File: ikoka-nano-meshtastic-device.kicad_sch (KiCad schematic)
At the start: 21 parts, among them J1 Qwiic_RA, J2 Solar, J3 Battery, J4 Battery, Q1 Q_PMOS_GSD, U1 Seeed Studio XIAO nRF52840, U2 E22-900M30S, U3 MT3608

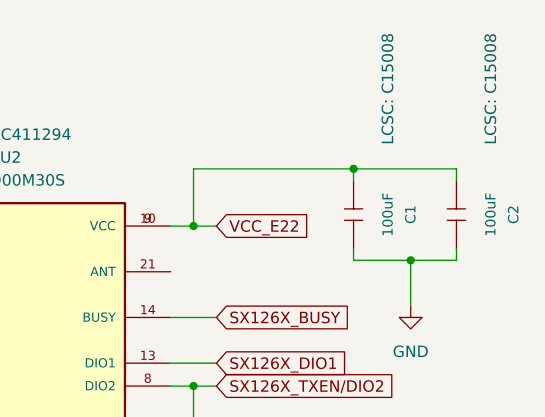
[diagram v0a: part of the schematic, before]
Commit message: Sync symbol libraries
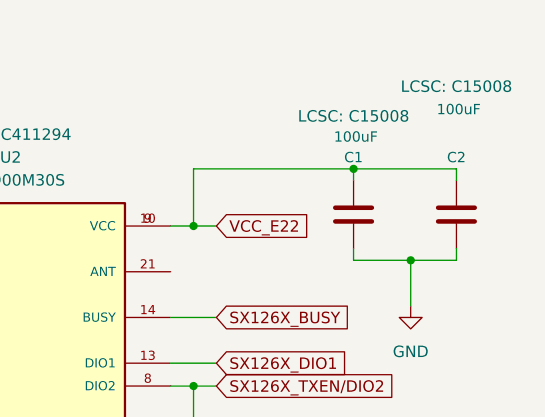
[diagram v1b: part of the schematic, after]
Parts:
- C1, C2: symbol OPL_Capacitor:CERAMIC-100UF-6.3V-20%-X5R_1206_ -> Device:C
- J1: footprint SparkFun-Connector:JST_SMD_1.0mm-4_RA -> SparkFun-Connector:JST_SMD_1.0mm-4_Black
- U2: Description_1 (none) -> SX1262 868/915 MHz 1w SPI LoRa Module
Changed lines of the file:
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@@
 	)
 	(symbol
-		(lib_name "GND_2")
 		(lib_id "power:GND")
 		(at 147.32 181.61 0)
@@
 			)
 		)
-		(property "Description" ""
+		(property "Description" "Power symbol creates a global label with name \"GND\" , ground"
 			(at 250.19 59.69 0)
 			(effects
@@
 			)
 		)
-		(property "Description" ""
+		(property "Description" "Power symbol creates a global label with name \"GND\" , ground"
 			(at 123.19 83.82 0)
 			(effects
@@
 			)
 		)
-		(property "Footprint" "SparkFun-Connector:JST_SMD_1.0mm-4_RA"
+		(property "Footprint" "SparkFun-Connector:JST_SMD_1.0mm-4_Black"
 			(at 53.34 180.34 0)
 			(effects
@@
 	)
 	(symbol
-		(lib_id "OPL_Capacitor:CERAMIC-100UF-6.3V-20%-X5R_1206_")
-		(at 255.27 49.53 90)
+		(lib_id "Device:C")
+		(at 255.27 49.53 180)
 		(unit 1)
 		(exclude_from_sim no)
@@
 		(dnp no)
 		(property "Reference" "C2"
-			(at 261.62 49.53 0)
+			(at 255.27 43.18 0)
 			(effects
 				(font
@@
 		)
 		(property "Value" "100uF"
-			(at 259.08 49.53 0)
+			(at 255.524 37.846 0)
 			(effects
 				(font
@@
 		)
 		(property "Footprint" "Capacitor_SMD:C_1206_3216Metric_Pad1.33x1.80mm_HandSolder"
+			(at 254.3048 45.72 0)
+			(effects
+				(font
+					(size 1.27 1.27)
+				)
+				(hide yes)
+			)
+		)
+		(property "Datasheet" "~"
 			(at 255.27 49.53 0)
 			(effects
@@
 			)
 		)
-		(property "Datasheet" ""
+		(property "Description" "Unpolarized capacitor"
 			(at 255.27 49.53 0)
 			(effects
@@
 			)
 		)
-		(property "Description" ""
-			(at 255.27 49.53 0)
-			(effects
-				(font
-					(size 1.27 1.27)
-				)
-				(hide yes)
-			)
-		)
 		(property "MPN" "CL31A107MQHNNNE"
-			(at 251.46 48.768 0)
+			(at 254.508 53.34 0)
 			(effects
 				(font
@@
 		)
 		(property "LCSC" "C15008"
-			(at 259.08 35.56 0)
+			(at 255.27 35.306 0)
 			(show_name yes)
 			(effects
@@
 	)
 	(symbol
-		(lib_name "GND_3")
 		(lib_id "power:GND")
 		(at 194.31 135.89 0)
@@
 			)
 		)
-		(property "Description" ""
+		(property "Description" "Power symbol creates a global label with name \"GND\" , ground"
 			(at 228.6 83.82 0)
 			(effects
@@
 			)
 		)
+		(property "Description_1" "\nSX1262 868/915 MHz 1w SPI LoRa Module\n"
+			(at 205.74 63.5 0)
+			(effects
+				(font
+					(size 1.27 1.27)
+				)
+				(justify bottom)
+				(hide yes)
+			)
+		)
 		(pin "8"
 		)
@@
 	)
 	(symbol
-		(lib_name "GND_1")
 		(lib_id "power:GND")
 		(at 90.17 184.15 0)
@@
 	)
 	(symbol
-		(lib_id "OPL_Capacitor:CERAMIC-100UF-6.3V-20%-X5R_1206_")
-		(at 243.84 49.53 90)
+		(lib_id "Device:C")
+		(at 243.84 49.53 180)
 		(unit 1)
 		(exclude_from_sim no)
@@
 		(dnp no)
 		(property "Reference" "C1"
-			(at 250.19 49.53 0)
+			(at 243.84 43.18 0)
 			(effects
 				(font
@@
 		)
 		(property "Value" "100uF"
-			(at 247.65 49.53 0)
+			(at 244.094 40.894 0)
 			(effects
 				(font
@@
 		)
 		(property "Footprint" "Capacitor_SMD:C_1206_3216Metric_Pad1.33x1.80mm_HandSolder"
+			(at 242.8748 45.72 0)
+			(effects
+				(font
+					(size 1.27 1.27)
+				)
+				(hide yes)
+			)
+		)
+		(property "Datasheet" "~"
 			(at 243.84 49.53 0)
 			(effects
@@
 			)
 		)
-		(property "Datasheet" ""
+		(property "Description" "Unpolarized capacitor"
 			(at 243.84 49.53 0)
 			(effects
@@
 			)
 		)
-		(property "Description" ""
-			(at 243.84 49.53 0)
-			(effects
-				(font
-					(size 1.27 1.27)
-				)
-				(hide yes)
-			)
-		)
 		(property "MPN" "CL31A107MQHNNNE"
-			(at 240.03 48.768 0)
+			(at 243.078 53.34 0)
 			(effects
 				(font
@@
 		)
 		(property "LCSC" "C15008"
-			(at 247.65 35.56 0)
+			(at 243.84 38.608 0)
 			(show_name yes)
 			(effects

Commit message: chore: Sync footprint libraries
Signed-off-by: Andrew Yong <me@ndoo.sg>
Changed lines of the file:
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@@
 (kicad_sch
-	(version 20231120)
+	(version 20250114)
 	(generator "eeschema")
-	(generator_version "8.0")
+	(generator_version "9.0")
 	(paper "A4")
 	(title_block
@@
 		(company "ndoo.sg")
 	)
+	(text "Nominal Vout: 5.4V"
+		(exclude_from_sim no)
+		(at 229.108 122.174 0)
+		(effects
+			(font
+				(size 1.27 1.27)
+			)
+		)
+	)
+	(text "Normally, gate would be pulled to ground to prevent floating.\nIn this case, VBUS is not pulled to ground because there is internal 100k pulldown on XIAO BLE.\nhttps://files.seeedstudio.com/wiki/XIAO-BLE/Seeed-Studio-XIAO-nRF52840-Sense-v1.1.pdf"
+		(exclude_from_sim no)
+		(at 109.22 133.35 0)
+		(effects
+			(font
+				(size 1.27 1.27)
+			)
+		)
+	)
 	(junction
 		(at 217.17 134.62)
@@
 		)
 	)
-	(text "Nominal Vout: 5.4V"
-		(exclude_from_sim no)
-		(at 229.108 122.174 0)
-		(effects
-			(font
-				(size 1.27 1.27)
-			)
-		)
-	)
-	(text "Normally, gate would be pulled to ground to prevent floating.\nIn this case, VBUS is not pulled to ground because there is internal 100k pulldown on XIAO BLE.\nhttps://files.seeedstudio.com/wiki/XIAO-BLE/Seeed-Studio-XIAO-nRF52840-Sense-v1.1.pdf"
-		(exclude_from_sim no)
-		(at 109.22 133.35 0)
-		(effects
-			(font
-				(size 1.27 1.27)
-			)
-		)
-	)
 	(global_label "VBAT"
 		(shape input)
@@
 		)
 	)
+	(embedded_fonts no)
 )

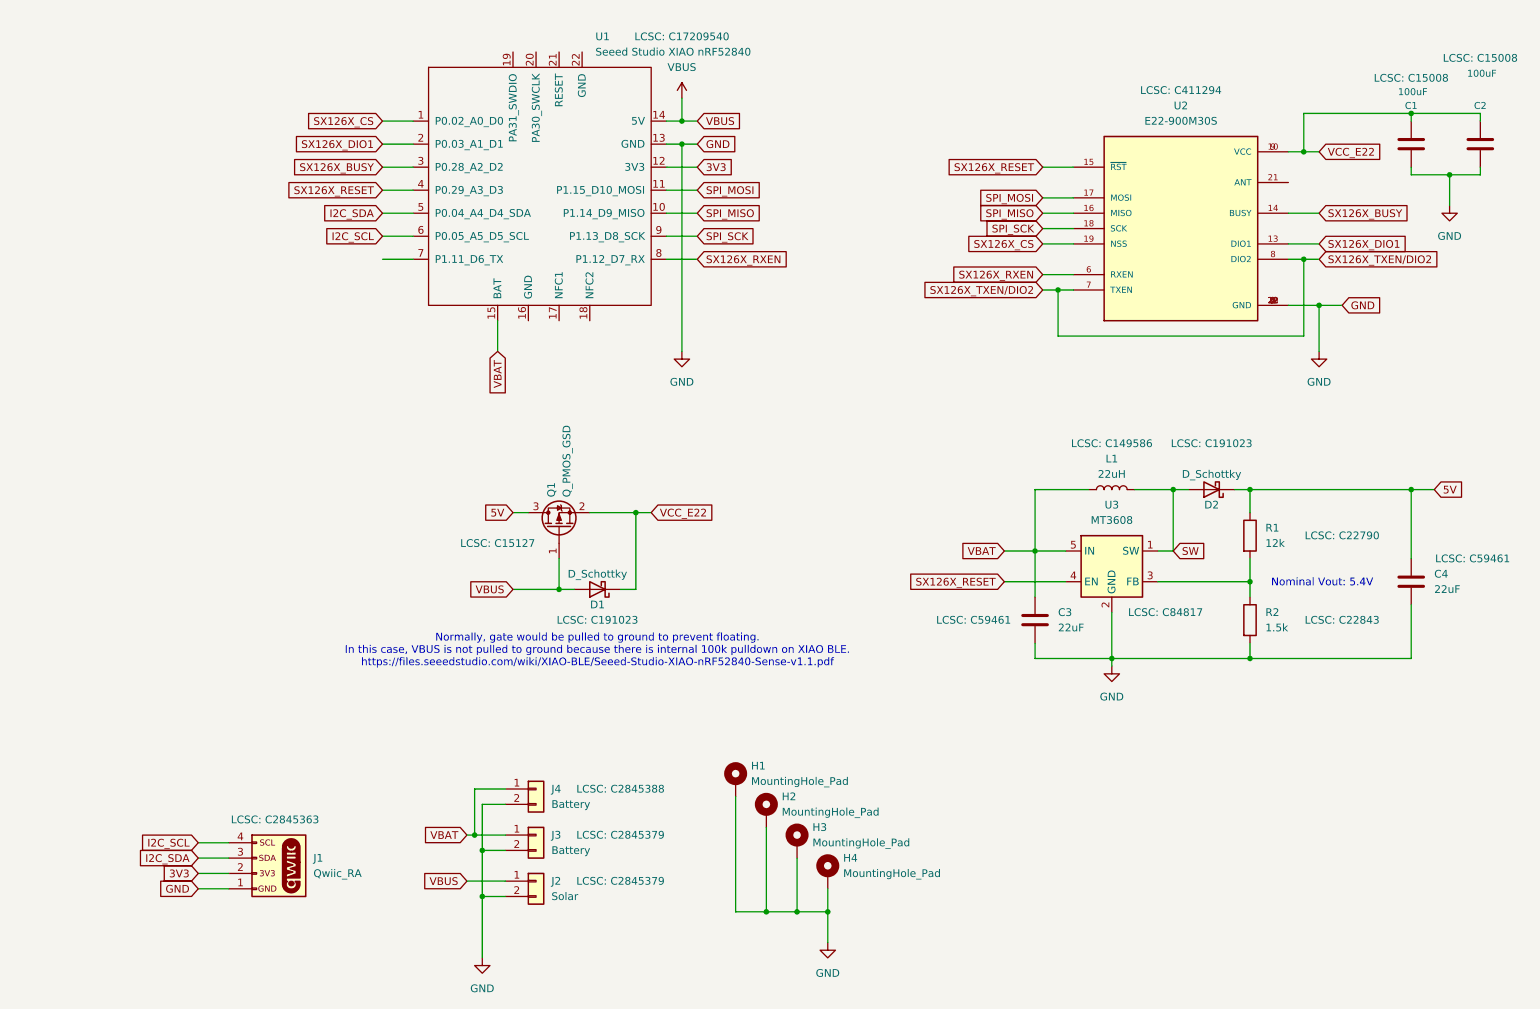
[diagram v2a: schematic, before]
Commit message: feat: Improve DC-DC converter and power path
- Update R1 and R2 resistors to match Ikoka Handheld values (300kΩ, 39kΩ respectively)
- Change E22 capacitors to 2x 47µF instead of 2x 100µF
- Change P-MOSFET load switch to switch input to DC-DC boost so that E22 supply is constant even when switching to USB power
- Add 300k pulldown on MT3608L enable pin to prevent it floating when Meshtastic firmware is not running
- Layout for above changes
- Move connectors flush with PCB edge

Fixes #11

Signed-off-by: Andrew Yong <me@ndoo.sg>
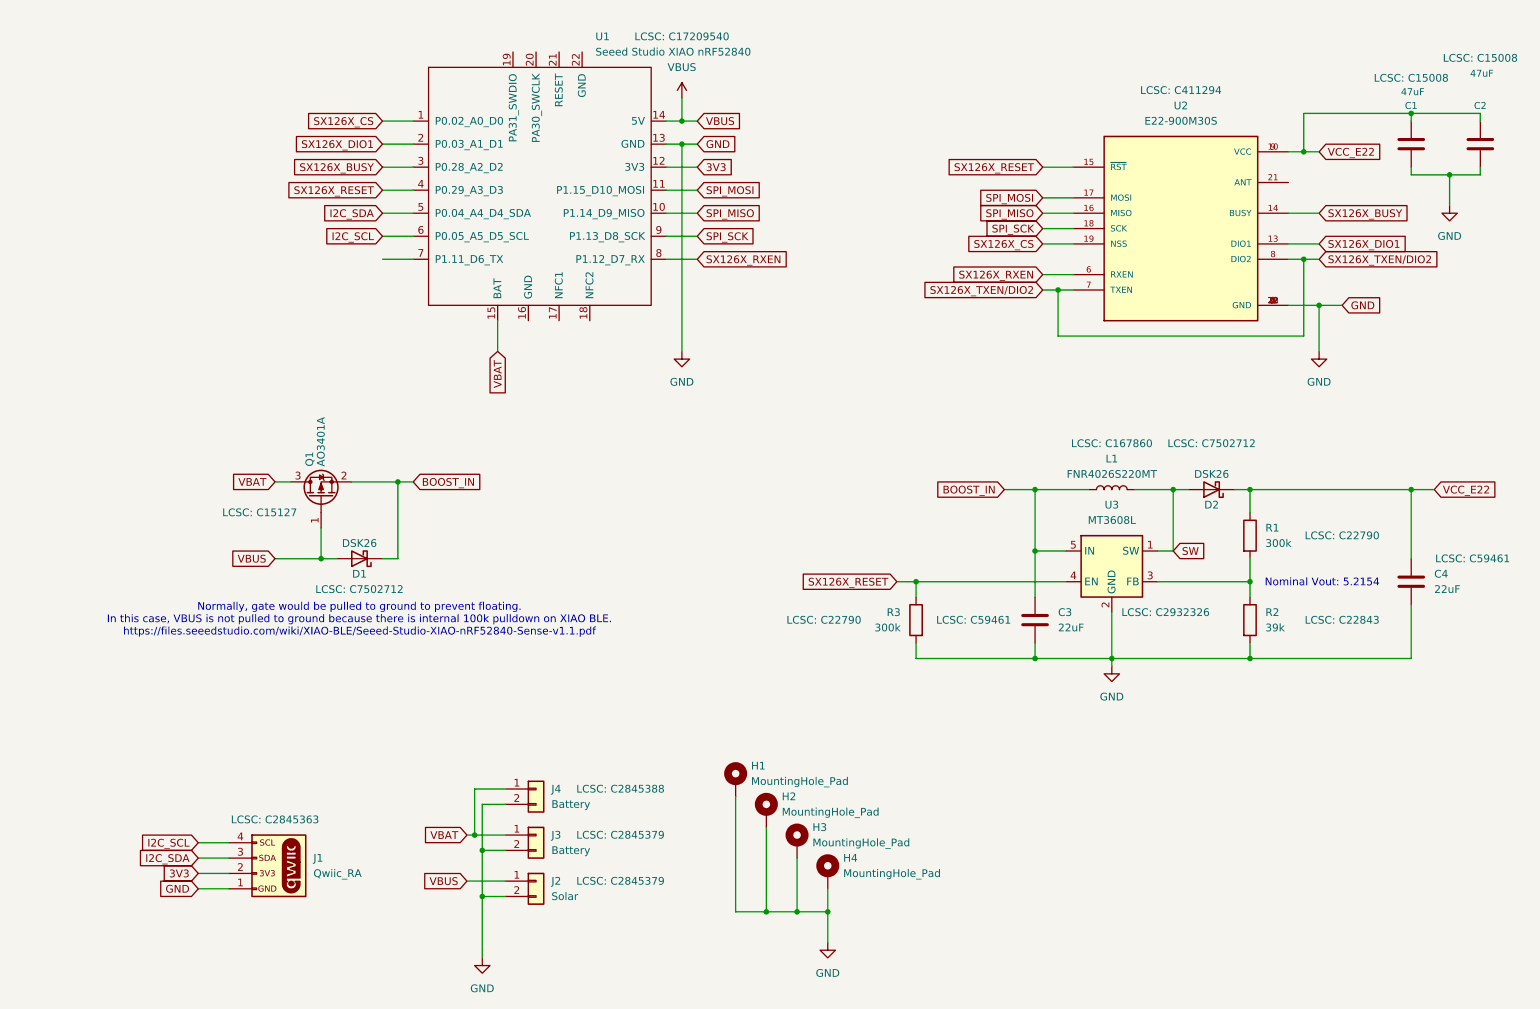
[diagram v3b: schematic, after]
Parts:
- added R3: 300k, Resistor_SMD:R_0603_1608Metric_Pad0.98x0.95mm_HandSolder, symbol Device:R
- C1, C2: value 100uF -> 47uF; footprint Capacitor_SMD:C_1206_3216Metric_Pad1.33x1.80mm_HandSolder -> Capacitor_SMD:C_0805_2012Metric_Pad1.18x1.45mm_HandSolder
- D1, D2: value D_Schottky -> DSK26; footprint Diode_SMD:D_SOD-323_HandSoldering -> Diode_SMD:D_SOD-123F; LCSC C191023 -> C7502712
- L1: value 22uH -> FNR4026S220MT; footprint Inductor_SMD:L_SXN_SMDRI64 -> Inductor_SMD:L_Changjiang_FNR4026S; LCSC C149586 -> C167860
- Q1: value Q_PMOS_GSD -> AO3401A; footprint Package_TO_SOT_SMD:SOT-23_Handsoldering -> Package_TO_SOT_SMD:SOT-23; symbol Device:Q_PMOS_GSD -> Transistor_FET:AO3401A
- R1: value 12k -> 300k
- R2: value 1.5k -> 39k
- U3: value MT3608 -> MT3608L; LCSC C84817 -> C2932326
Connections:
- net GND: now also R3.2
- net SX126X_RESET: now also R3.1
- net VBAT: now also Q1.3 (D); no longer C3.1, L1.1, U3.5 (IN)
- net VCC_E22: now also C4.1, D2.1 (K), R1.1; no longer D1.1 (K), Q1.2 (S)
- removed net 5V: C4.1, D2.1 (K), Q1.3 (D), R1.1
- new net BOOST_IN: C3.1, D1.1 (K), L1.1, Q1.2 (S), U3.5 (IN)
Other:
- note added: "Nominal Vout: 5.2154"
- note removed: "Nominal Vout: 5.4V"
- moved on the sheet: D1, Q1

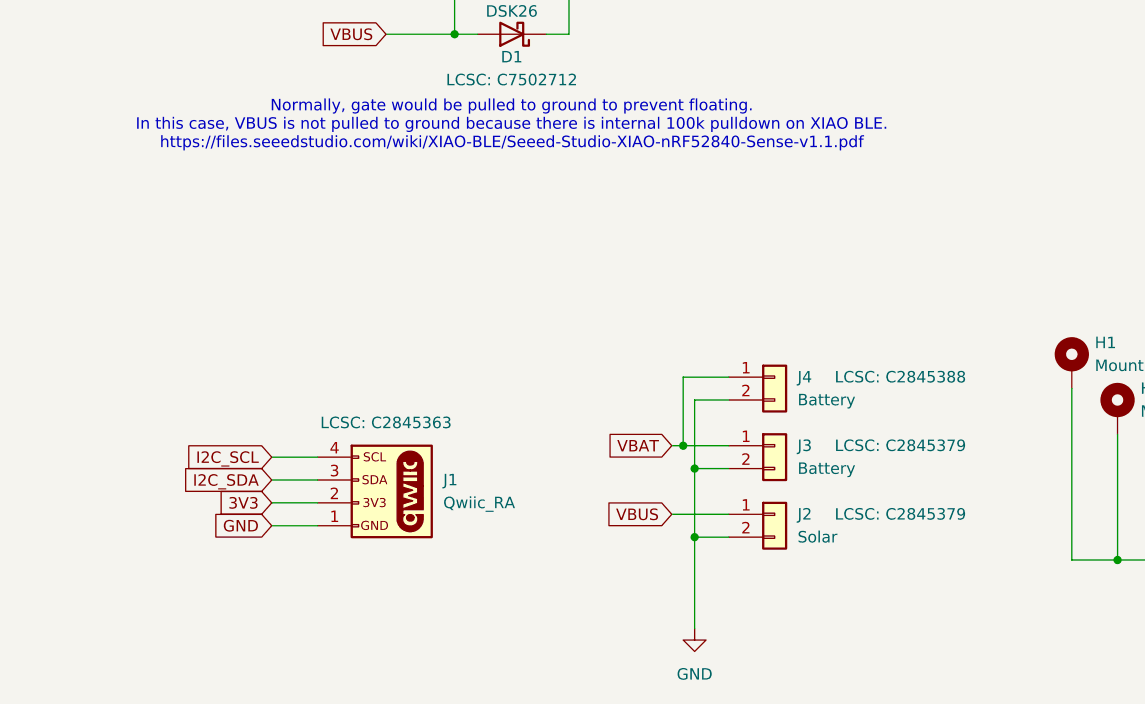
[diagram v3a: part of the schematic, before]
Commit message: chore: Use correct Kicad connector symbols and ground MountingPins
Signed-off-by: Andrew Yong <me@ndoo.sg>
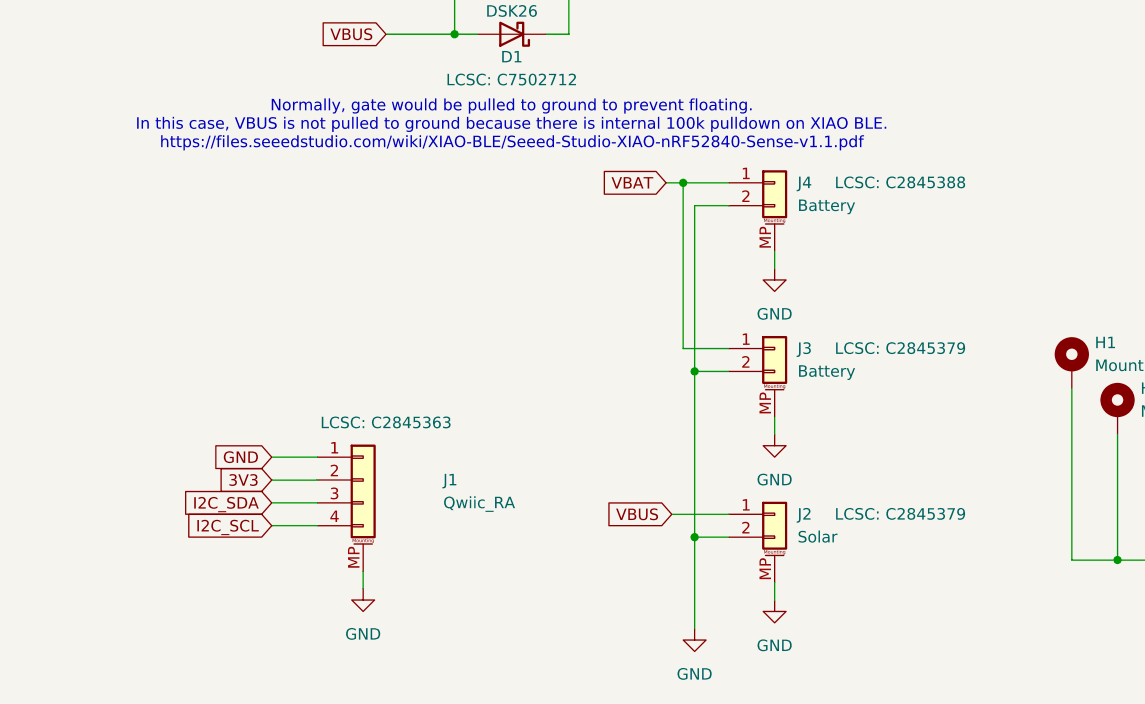
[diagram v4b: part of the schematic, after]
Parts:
- J1: footprint SparkFun-Connector:JST_SMD_1.0mm-4_Black -> Connector_JST:JST_SH_SM04B-SRSS-TB_1x04-1MP_P1.00mm_Horizontal; symbol SparkFun-Connector:Qwiic_Right_Angle -> Connector_Generic_MountingPin:Conn_01x04_MountingPin
- J2, J3, J4: symbol Connector_Generic:Conn_01x02 -> Connector_Generic_MountingPin:Conn_01x02_MountingPin
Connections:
- net GND: now also J1.MP (MountPin), J2.MP (MountPin), J3.MP (MountPin), J4.MP (MountPin)

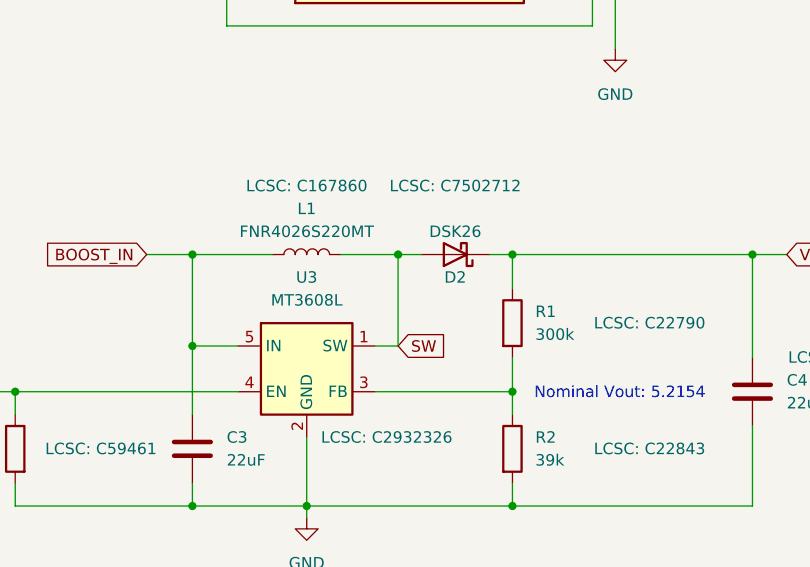
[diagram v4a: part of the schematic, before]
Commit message: feat: Improve boost converter part selection
- Change inductor from 22uH FNR4026S220MT to 2.2uH FXL0420-2R2-M
- Change MT3608L to MT3608B

Signed-off-by: Andrew Yong <me@ndoo.sg>
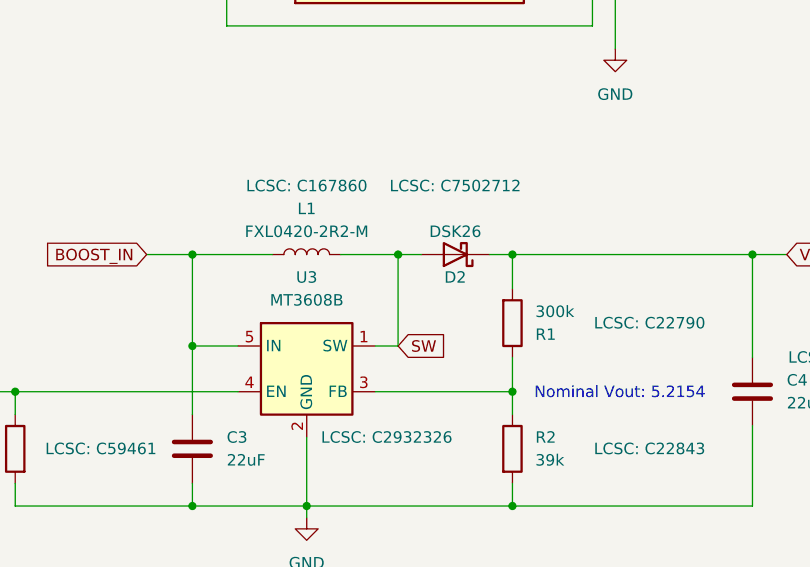
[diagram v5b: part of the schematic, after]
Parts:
- L1: value FNR4026S220MT -> FXL0420-2R2-M; footprint Inductor_SMD:L_Changjiang_FNR4026S -> Inductor_SMD:L_Changjiang_FXL0420
- U3: value MT3608L -> MT3608B
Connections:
- net VCC_E22: now also R1.2; no longer R1.1
- net at R2.1, U3.3 (FB): now also R1.1; no longer R1.2
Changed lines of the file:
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@@
 			)
 		)
-		(property "Value" "FNR4026S220MT"
+		(property "Value" "FXL0420-2R2-M"
 			(at 194.31 104.14 90)
 			(effects
@@
 			)
 		)
-		(property "Footprint" "Inductor_SMD:L_Changjiang_FNR4026S"
+		(property "Footprint" "Inductor_SMD:L_Changjiang_FXL0420"
 			(at 194.31 106.68 0)
 			(effects
@@
 			)
 		)
-		(property "Value" "MT3608L"
+		(property "Value" "MT3608B"
 			(at 194.31 111.76 0)
 			(effects
@@
 		(lib_id "Device:R")
 		(at 217.17 114.3 0)
+		(mirror x)
 		(unit 1)
 		(exclude_from_sim no)
@@
 		(dnp no)
 		(property "Reference" "R1"
-			(at 219.71 113.0299 0)
+			(at 219.71 115.5701 0)
 			(effects
 				(font
@@
 		)
 		(property "Value" "300k"
-			(at 219.71 115.5699 0)
-			(effects
-				(font
+			(at 219.71 113.0301 0)
+			(effects
+				(font
